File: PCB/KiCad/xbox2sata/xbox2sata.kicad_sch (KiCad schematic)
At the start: 47 parts, among them IC1 TLV1117LV12DCYR, J1 61203921621, J2 67800-8025, J3 90151-2140, U5 88SA8052, Y1 ABLS-25.000MHZ-B4-F-T

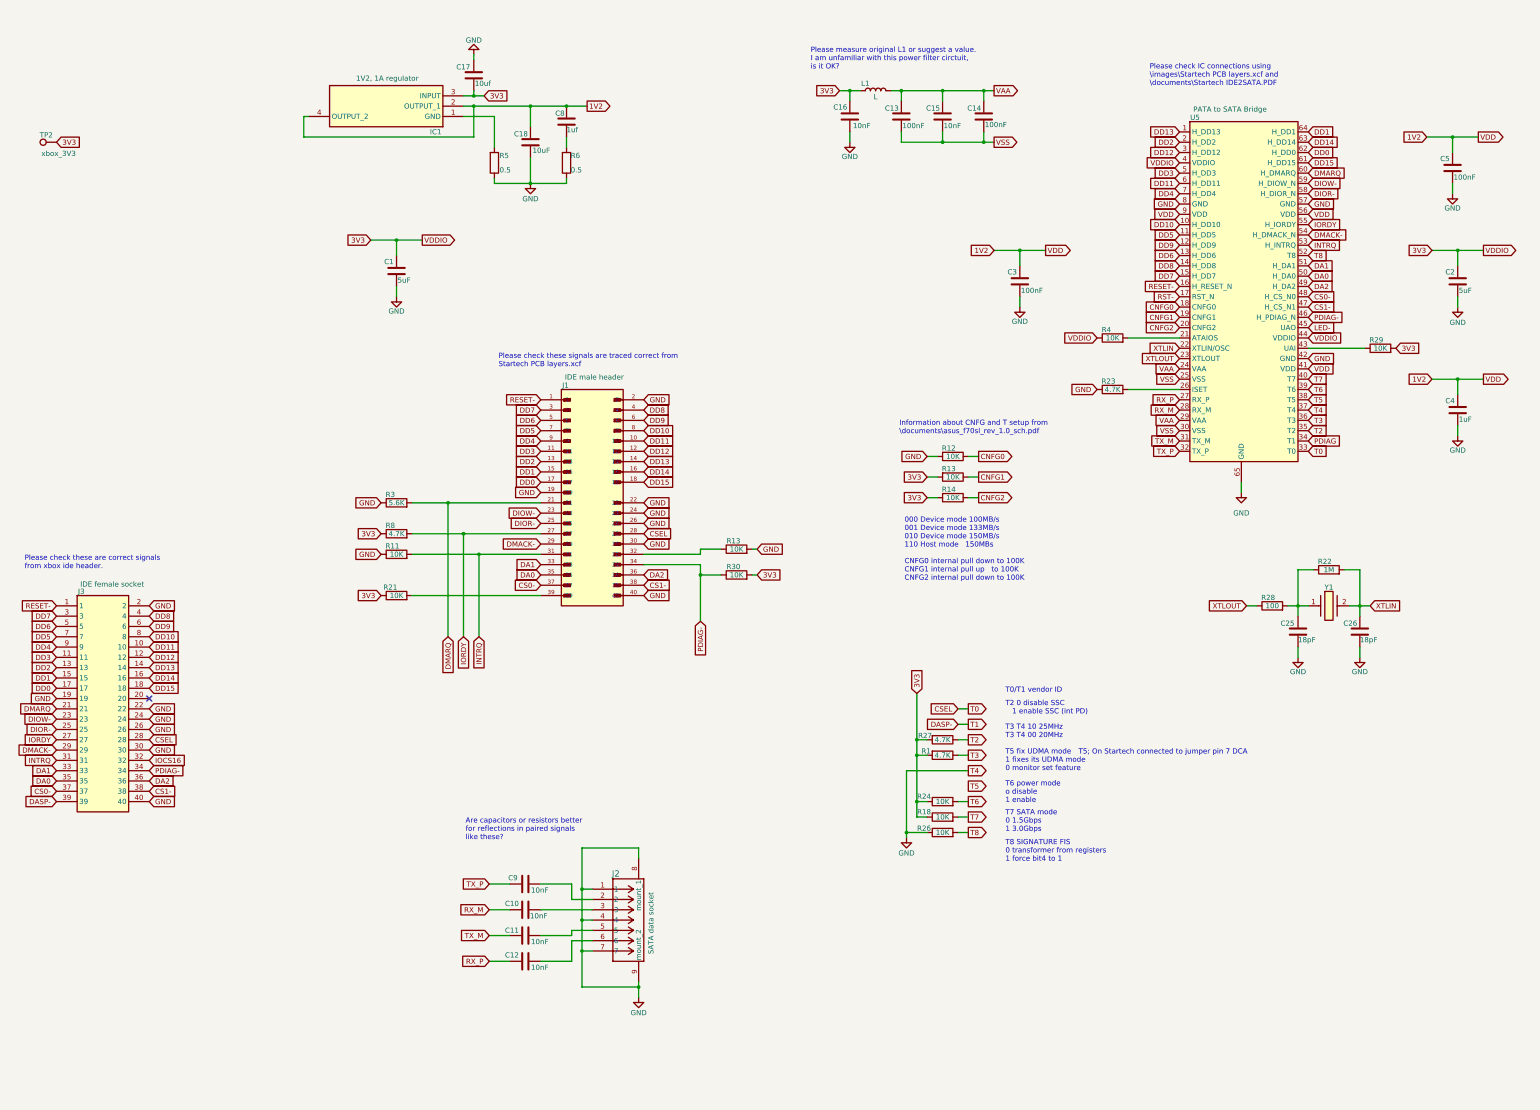
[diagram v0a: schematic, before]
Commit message: oscillator circuit corrected
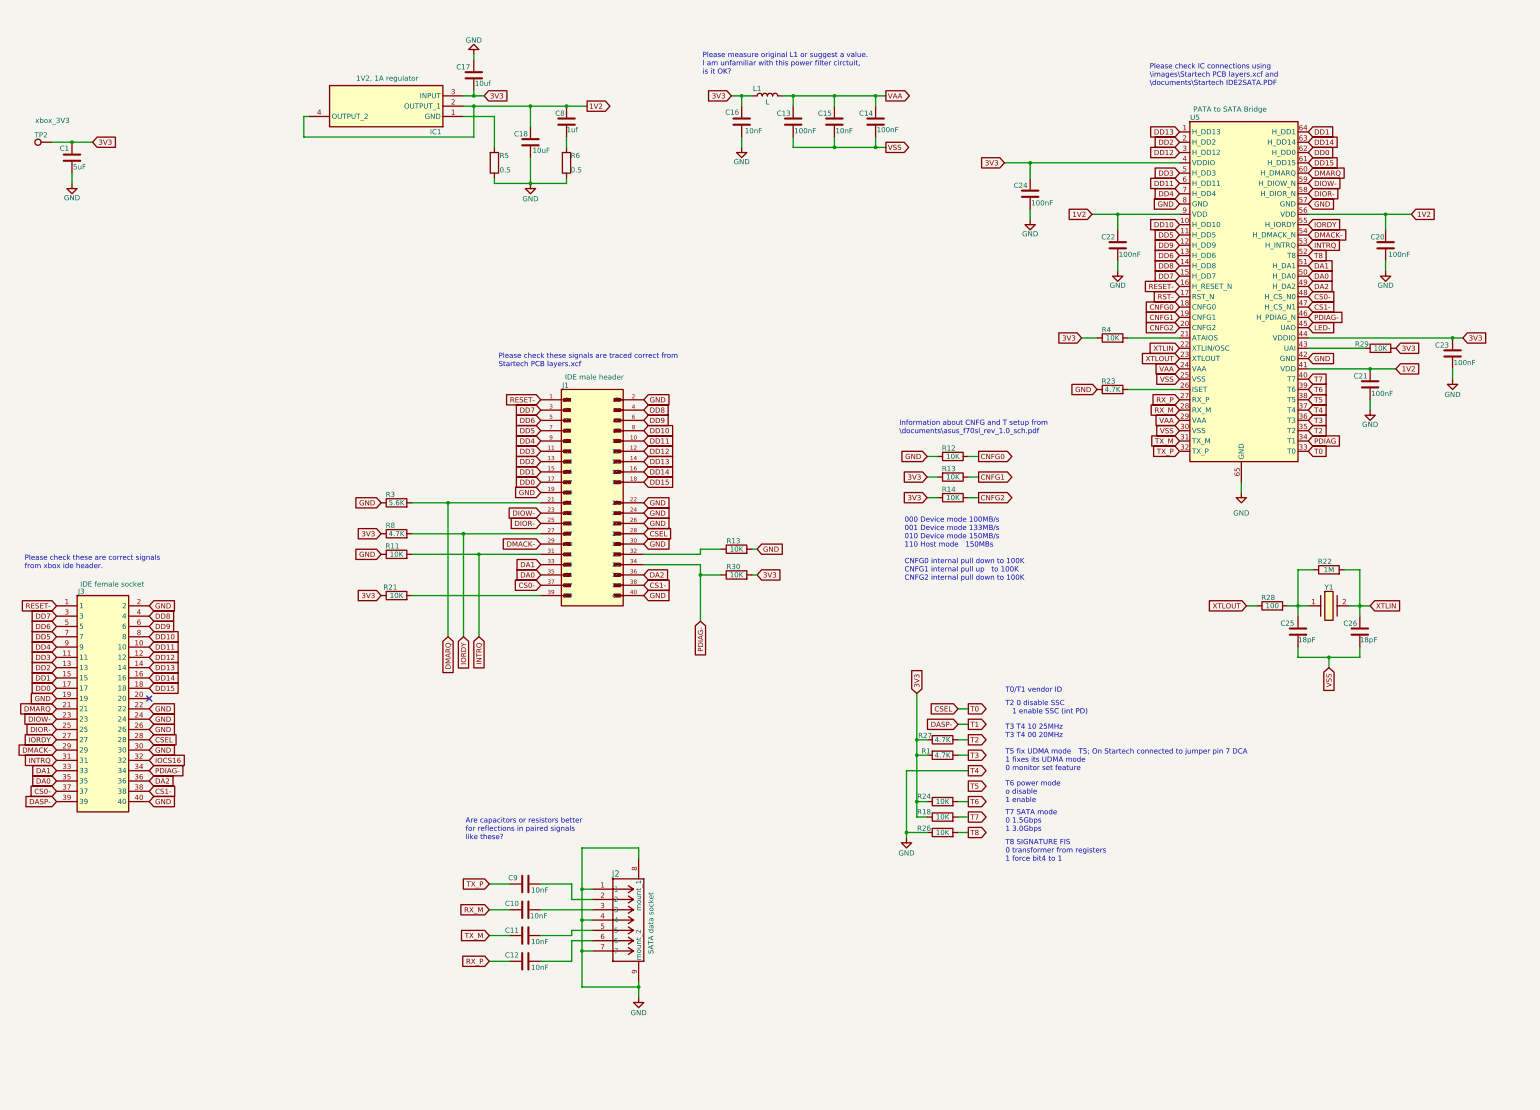
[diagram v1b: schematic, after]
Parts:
- added C24: 100nF, Capacitor_SMD:C_0402_1005Metric_Pad0.74x0.62mm_HandSolder, symbol Device:C
- C21: renamed from C4; value 1uF -> 100nF
- C23: renamed from C2; value 5uF -> 100nF
- renumbered C5 to C20, C3 to C22
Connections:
- net 3V3: now also C24.1
- net GND: now also C24.2; no longer C25.2, C26.2
- net VSS: now also C25.2, C26.2
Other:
- moved on the sheet: C1, C13, C14, C15, C16, C20, C21, C22, C23, L1, TP2

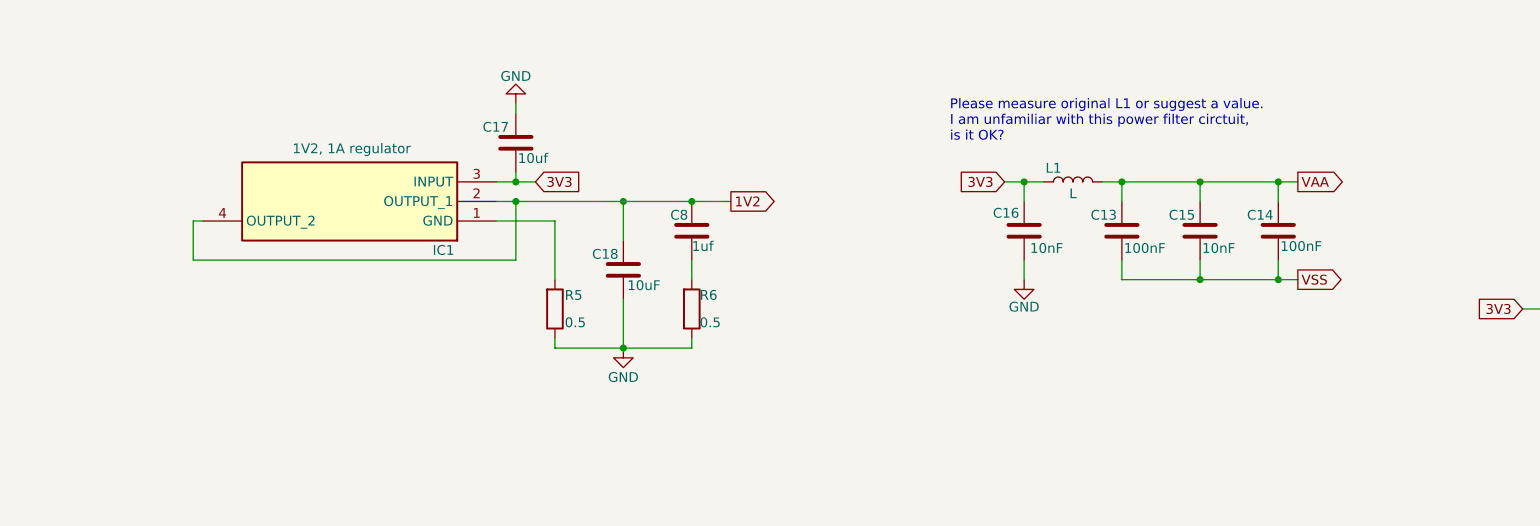
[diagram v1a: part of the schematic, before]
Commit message: Variable voltage regulator changed to fixed 1V2
Variable voltage regulator changed to fixed 1V2 regulator. L1 is a ferrite bead not a inductor.
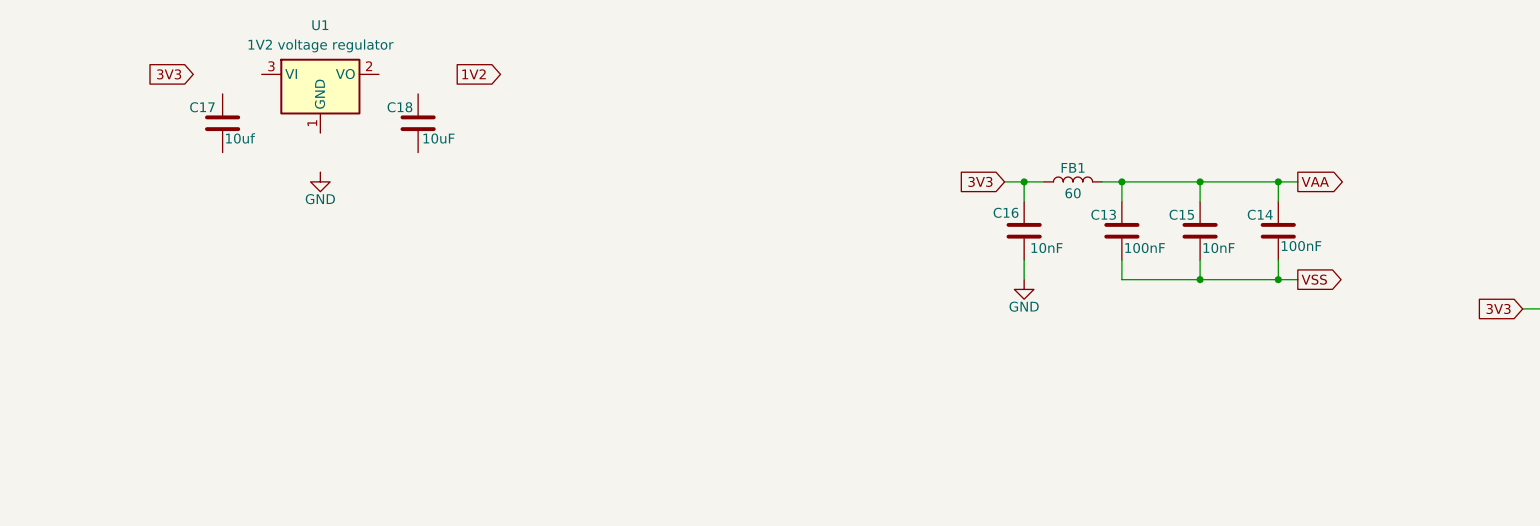
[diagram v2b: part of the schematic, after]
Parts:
- removed C8: 1uf, symbol Device:C
- removed IC1: TLV1117LV12DCYR, xbox2sata:SOT230P700X180-4N, symbol xbox2sata:TLV1117LV12DCYR
- removed R5, R6: 0.5, symbol Device:R
- added U1: 1V2 voltage regulator, Package_TO_SOT_SMD:SOT-223-3_TabPin2, symbol xbox2sata:1V2_voltage_regulator
- FB1: renamed from L1; value L -> 60
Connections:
- net 1V2: no longer C18.1
- net 3V3: no longer C17.1
- net GND: no longer C17.2, C18.2
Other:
- note removed: "Please measure original L1 or suggest a value. I am unfamiliar with this power filter circtuit, is it OK?"
- moved on the sheet: C17, C18

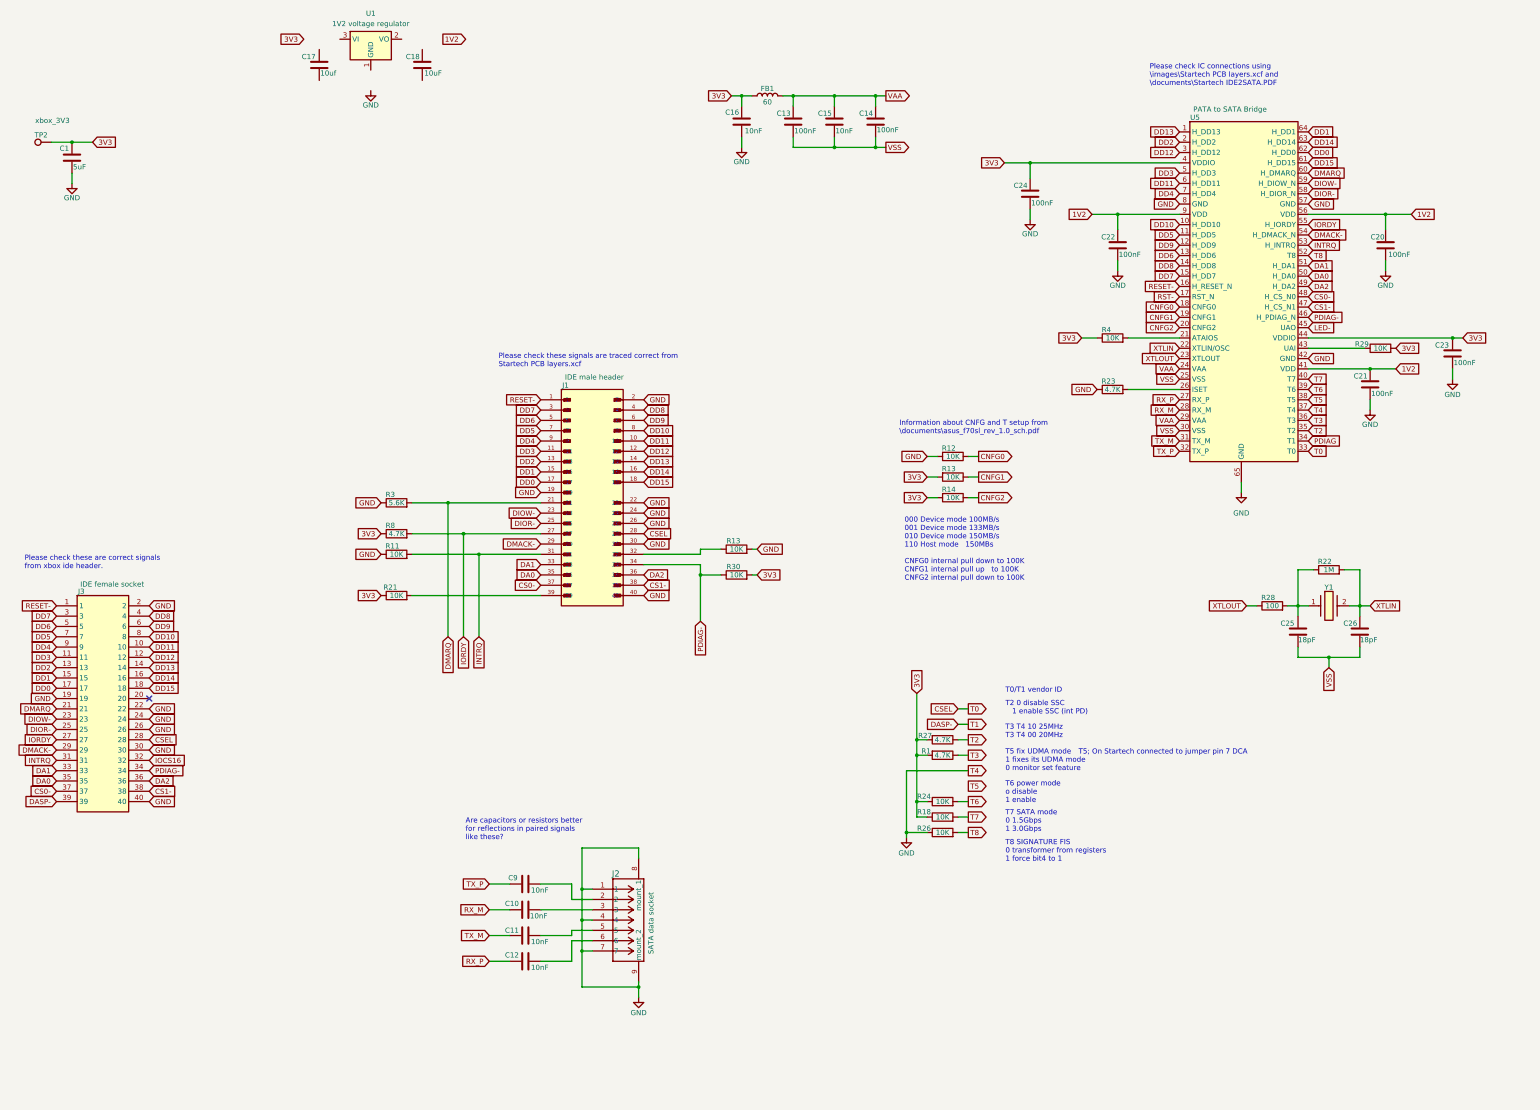
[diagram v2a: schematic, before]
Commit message: IDE pins changes
IDE pins 32 and 34 on xbox only connect to test points. Therefore connected to ground.
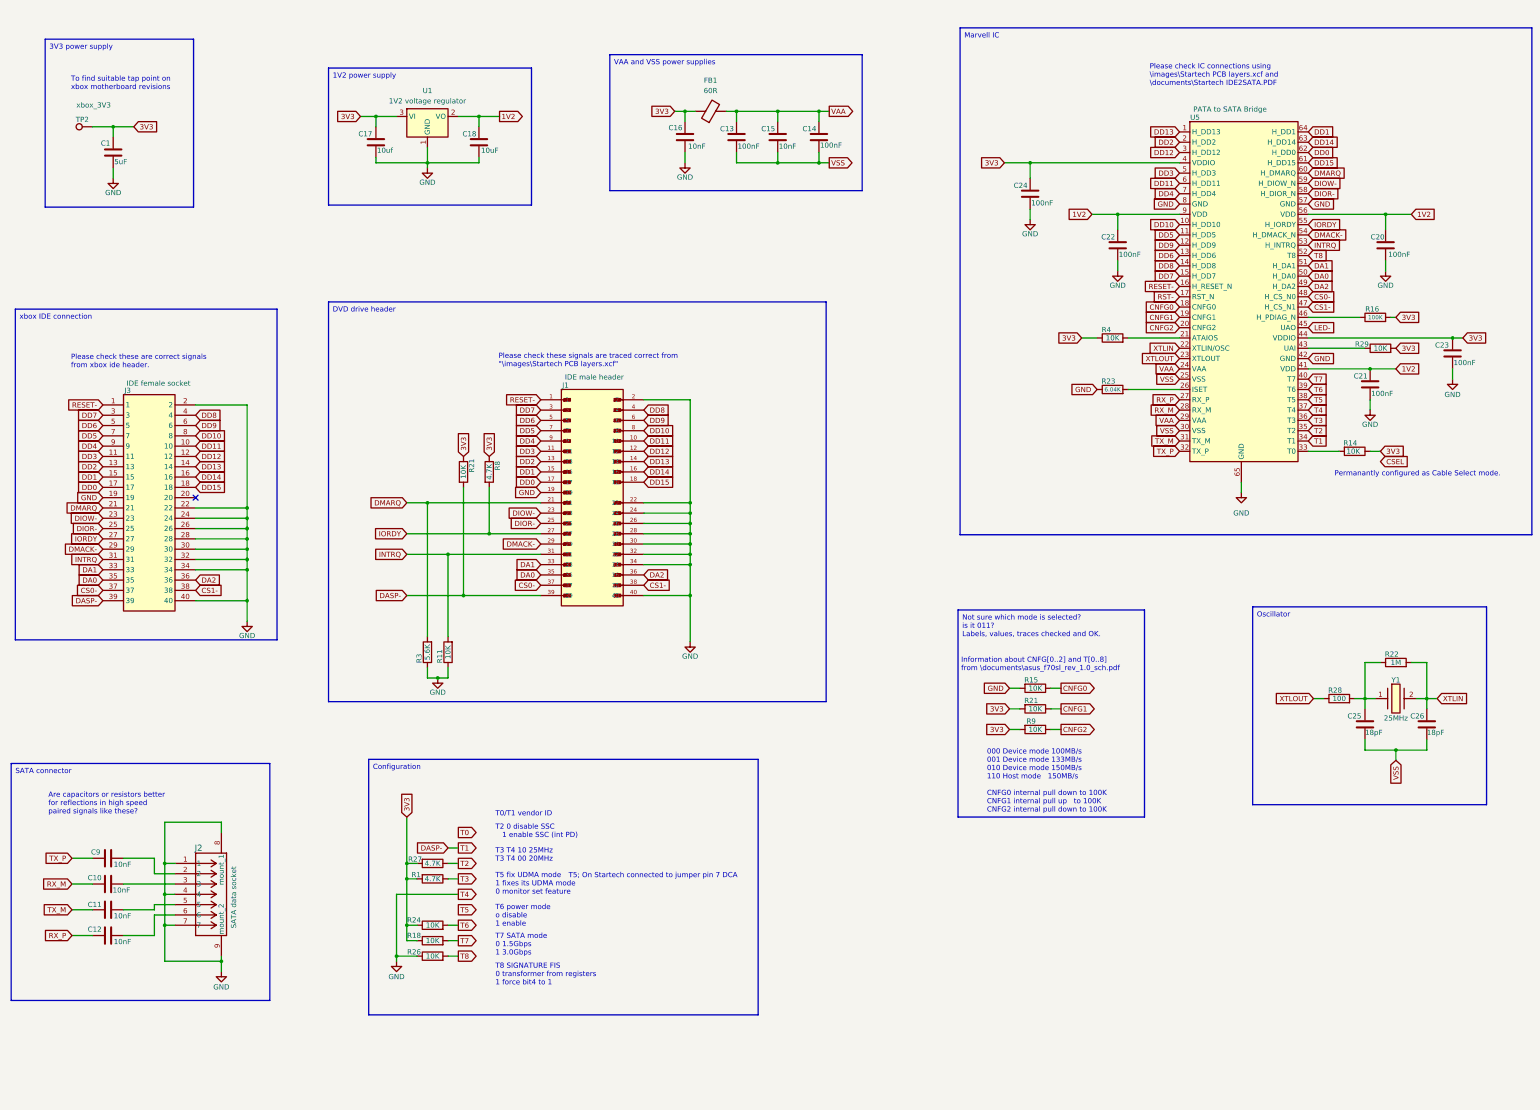
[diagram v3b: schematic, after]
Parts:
- removed FB1: 60, Inductor_SMD:L_0402_1005Metric_Pad0.77x0.64mm_HandSolder, symbol Device:L
- removed R13: 10K, Resistor_SMD:R_0402_1005Metric_Pad0.72x0.64mm_HandSolder, symbol Device:R
- added FB1: 60R, symbol Device:FerriteBead
- added R14: 10K, symbol Device:R
- R16: renamed from R30; value 10K -> 100K
- R23: value 4.7K -> 6.04K
- Y1: value ABLS-25.000MHZ-B4-F-T -> 25MHz
- renumbered R12 to R15, R13 to R21, R14 to R9
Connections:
- net IOCS16 is gone; now on net GND: J3.32
- net PDIAG is gone; now on net DASP-: U5.34 (T1)
- net 1V2: now also C18.1, U1.2 (VO)
- net 3V3: now also C17.2, U1.3 (VI), FB1.1, R14.1
- net CSEL: no longer J1.28, J3.28, U5.33 (T0)
- net DASP-: now also J1.39, R21.2
- net GND: now also C17.1, C18.2, J1.28, J1.32, J1.34, J3.28, J3.34, U1.1 (GND)
- net VAA: now also FB1.2
- net PDIAG-: no longer names the net of R16.1, U5.46 (H_PDIAG_N)
- net PDIAG-: no longer J1.34, J3.34
- new net: R14.2, U5.33 (T0)
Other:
- note added: "Are capacitors or resistors better for reflections in high speed paired signals like these?"
- note added: "Information about CNFG[0..2] and T[0..8] from \documents\asus_f70sl_rev_1.0_sch.pdf"
- note added: "Permanantly configured as Cable Select mode."
- note added: "Please check these signals are traced correct from "\images\Startech PCB layers.xcf""
- note added: "To find suitable tap point on xbox motherboard revisions"
- note removed: "Are capacitors or resistors better for reflections in paired signals like these?"
- note removed: "Information about CNFG and T setup from \documents\asus_f70sl_rev_1.0_sch.pdf"
- note removed: "Please check these signals are traced correct from Startech PCB layers.xcf"
- moved on the sheet: C1, C10, C11, C12, C13, C14, C15, C16, C17, C18, C25, C26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
